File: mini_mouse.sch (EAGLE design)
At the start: 32 parts, among them IC1 PIC18F4550_TQFP, IC3 LP2950CDT-5.0, IC4 L293D

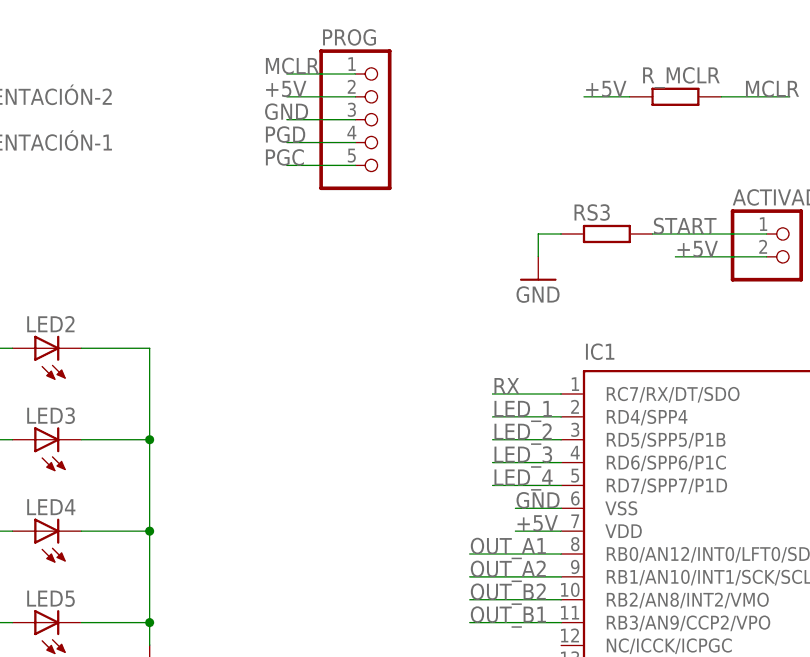
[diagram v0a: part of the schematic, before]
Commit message: Leds re-acomodados
Se  acomodaron los LEDS del lado derecho de la placa.
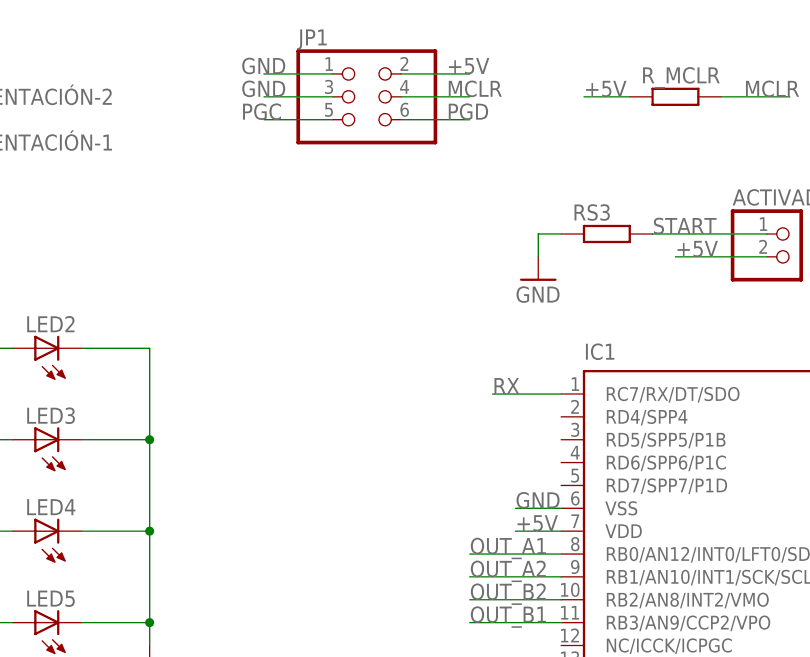
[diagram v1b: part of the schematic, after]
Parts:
- removed PROG: (no value), pinhead:PINHD-1X5
- added JP1: (no value), pinhead:PINHD-2X3
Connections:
- net +5V: now also JP1.2; no longer PROG.2
- net GND: now also JP1.1, JP1.3; no longer PROG.3
- net LED_1: no longer IC1.RD4/SPP4
- net LED_2: no longer IC1.RD5/SPP5/P1B
- net LED_3: no longer IC1.RD6/SPP6/P1C
- net LED_4: no longer IC1.RD7/SPP7/P1D
- net MCLR: now also JP1.4; no longer PROG.1
- net PGC: now also JP1.5; no longer PROG.5
- net PGD: now also JP1.6; no longer PROG.4
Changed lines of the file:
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@@
 <part name="C2" library="rcl" library_urn="urn:adsk.eagle:library:334" deviceset="C-EU" device="C0603" package3d_urn="urn:adsk.eagle:package:23616/2"/>
 <part name="R_MCLR" library="rcl" library_urn="urn:adsk.eagle:library:334" deviceset="R-EU_" device="R0603" package3d_urn="urn:adsk.eagle:package:23555/3"/>
-<part name="PROG" library="pinhead" library_urn="urn:adsk.eagle:library:325" deviceset="PINHD-1X5" device="" package3d_urn="urn:adsk.eagle:package:22469/2"/>
 <part name="GND1" library="supply1" library_urn="urn:adsk.eagle:library:371" deviceset="GND" device=""/>
 <part name="GND2" library="supply1" library_urn="urn:adsk.eagle:library:371" deviceset="GND" device=""/>
@@
 <part name="C4" library="rcl" library_urn="urn:adsk.eagle:library:334" deviceset="CPOL-EU" device="E5-6" package3d_urn="urn:adsk.eagle:package:23368/1"/>
 <part name="COMUNICACION" library="pinhead" library_urn="urn:adsk.eagle:library:325" deviceset="PINHD-2X2" device="" package3d_urn="urn:adsk.eagle:package:22455/2"/>
+<part name="JP1" library="pinhead" library_urn="urn:adsk.eagle:library:325" deviceset="PINHD-2X3" device="" package3d_urn="urn:adsk.eagle:package:22462/2"/>
 </parts>
 <sheets>
@@
 <attribute name="VALUE" x="107.95" y="156.718" size="1.778" layer="96"/>
 </instance>
-<instance part="PROG" gate="A" x="78.74" y="157.48">
-<attribute name="NAME" x="72.39" y="165.735" size="1.778" layer="95"/>
-<attribute name="VALUE" x="72.39" y="147.32" size="1.778" layer="96"/>
-</instance>
 <instance part="GND1" gate="1" x="12.7" y="149.86">
 <attribute name="VALUE" x="10.16" y="147.32" size="1.778" layer="96"/>
@@
 <attribute name="NAME" x="227.33" y="160.655" size="1.778" layer="95"/>
 <attribute name="VALUE" x="227.33" y="149.86" size="1.778" layer="96"/>
+</instance>
+<instance part="JP1" gate="A" x="76.2" y="160.02">
+<attribute name="NAME" x="69.85" y="165.735" size="1.778" layer="95"/>
+<attribute name="VALUE" x="69.85" y="152.4" size="1.778" layer="96"/>
 </instance>
 </instances>
@@
 <net name="MCLR" class="0">
 <segment>
-<pinref part="PROG" gate="A" pin="1"/>
-<wire x1="76.2" y1="162.56" x2="68.58" y2="162.56" width="0.1524" layer="91"/>
-<label x="66.04" y="162.56" size="1.778" layer="95"/>
-</segment>
-<segment>
 <pinref part="IC1" gate="G$1" pin="!MCLR!/VPP/RE3"/>
 <wire x1="99.06" y1="83.82" x2="91.44" y2="83.82" width="0.1524" layer="91"/>
@@
 <label x="119.38" y="160.02" size="1.778" layer="95"/>
 </segment>
+<segment>
+<pinref part="JP1" gate="A" pin="4"/>
+<wire x1="81.28" y1="160.02" x2="88.9" y2="160.02" width="0.1524" layer="91"/>
+<label x="86.36" y="160.02" size="1.778" layer="95"/>
+</segment>
 </net>
 <net name="+5V" class="0">
-<segment>
-<pinref part="PROG" gate="A" pin="2"/>
-<wire x1="76.2" y1="160.02" x2="68.58" y2="160.02" width="0.1524" layer="91"/>
-<label x="66.04" y="160.02" size="1.778" layer="95"/>
-</segment>
 <segment>
 <pinref part="IC1" gate="G$1" pin="VDD"/>
@@
 <label x="220.98" y="157.48" size="1.778" layer="95"/>
 </segment>
+<segment>
+<pinref part="JP1" gate="A" pin="2"/>
+<wire x1="81.28" y1="162.56" x2="88.9" y2="162.56" width="0.1524" layer="91"/>
+<label x="86.36" y="162.56" size="1.778" layer="95"/>
+</segment>
 </net>
 <net name="PGD" class="0">
-<segment>
-<pinref part="PROG" gate="A" pin="4"/>
-<wire x1="76.2" y1="154.94" x2="68.58" y2="154.94" width="0.1524" layer="91"/>
-<label x="66.04" y="154.94" size="1.778" layer="95"/>
-</segment>
 <segment>
 <pinref part="IC1" gate="G$1" pin="RB7/BKI3/PGD"/>
@@
 <label x="91.44" y="86.36" size="1.778" layer="95"/>
 </segment>
+<segment>
+<pinref part="JP1" gate="A" pin="6"/>
+<wire x1="81.28" y1="157.48" x2="88.9" y2="157.48" width="0.1524" layer="91"/>
+<label x="86.36" y="157.48" size="1.778" layer="95"/>
+</segment>
 </net>
 <net name="PGC" class="0">
-<segment>
-<pinref part="PROG" gate="A" pin="5"/>
-<wire x1="76.2" y1="152.4" x2="68.58" y2="152.4" width="0.1524" layer="91"/>
-<label x="66.04" y="152.4" size="1.778" layer="95"/>
-</segment>
 <segment>
 <pinref part="IC1" gate="G$1" pin="RB6/KBI2/PGC"/>
 <wire x1="99.06" y1="88.9" x2="91.44" y2="88.9" width="0.1524" layer="91"/>
 <label x="91.44" y="88.9" size="1.778" layer="95"/>
+</segment>
+<segment>
+<pinref part="JP1" gate="A" pin="5"/>
+<wire x1="73.66" y1="157.48" x2="66.04" y2="157.48" width="0.1524" layer="91"/>
+<label x="63.5" y="157.48" size="1.778" layer="95"/>
 </segment>
 </net>
@@
 <wire x1="152.4" y1="149.86" x2="152.4" y2="152.4" width="0.1524" layer="91"/>
 <junction x="152.4" y="152.4"/>
-</segment>
-<segment>
-<pinref part="PROG" gate="A" pin="3"/>
-<wire x1="76.2" y1="157.48" x2="68.58" y2="157.48" width="0.1524" layer="91"/>
-<label x="66.04" y="157.48" size="1.778" layer="95"/>
 </segment>
 <segment>
@@
 <label x="220.98" y="154.94" size="1.778" layer="95"/>
 </segment>
+<segment>
+<pinref part="JP1" gate="A" pin="1"/>
+<wire x1="73.66" y1="162.56" x2="66.04" y2="162.56" width="0.1524" layer="91"/>
+<label x="63.5" y="162.56" size="1.778" layer="95"/>
+</segment>
+<segment>
+<pinref part="JP1" gate="A" pin="3"/>
+<wire x1="73.66" y1="160.02" x2="66.04" y2="160.02" width="0.1524" layer="91"/>
+<label x="63.5" y="160.02" size="1.778" layer="95"/>
+</segment>
 </net>
 <net name="OSC2" class="0">
@@
 <net name="LED_1" class="0">
 <segment>
-<pinref part="IC1" gate="G$1" pin="RD4/SPP4"/>
-<wire x1="99.06" y1="124.46" x2="91.44" y2="124.46" width="0.1524" layer="91"/>
-<label x="91.44" y="124.46" size="1.778" layer="95"/>
-</segment>
-<segment>
 <pinref part="R_L1" gate="G$1" pin="1"/>
 <wire x1="22.86" y1="132.08" x2="17.78" y2="132.08" width="0.1524" layer="91"/>
@@
 <net name="LED_2" class="0">
 <segment>
-<pinref part="IC1" gate="G$1" pin="RD5/SPP5/P1B"/>
-<wire x1="99.06" y1="121.92" x2="91.44" y2="121.92" width="0.1524" layer="91"/>
-<label x="91.44" y="121.92" size="1.778" layer="95"/>
-</segment>
-<segment>
 <pinref part="R_L2" gate="G$1" pin="1"/>
 <wire x1="22.86" y1="121.92" x2="17.78" y2="121.92" width="0.1524" layer="91"/>
@@
 <net name="LED_3" class="0">
 <segment>
-<pinref part="IC1" gate="G$1" pin="RD6/SPP6/P1C"/>
-<wire x1="99.06" y1="119.38" x2="91.44" y2="119.38" width="0.1524" layer="91"/>
-<label x="91.44" y="119.38" size="1.778" layer="95"/>
-</segment>
-<segment>
 <pinref part="R_L3" gate="G$1" pin="1"/>
 <wire x1="22.86" y1="111.76" x2="17.78" y2="111.76" width="0.1524" layer="91"/>
@@
 <net name="LED_4" class="0">
 <segment>
-<pinref part="IC1" gate="G$1" pin="RD7/SPP7/P1D"/>
-<wire x1="99.06" y1="116.84" x2="91.44" y2="116.84" width="0.1524" layer="91"/>
-<label x="91.44" y="116.84" size="1.778" layer="95"/>
-</segment>
-<segment>
 <pinref part="R_L4" gate="G$1" pin="1"/>

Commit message: Actualización Board
Se actualizo la distribucion de componentes, se cambio el tamaño de los package de las resistencias y capacitores smd y se modifico la forma de la tarjeta.
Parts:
- removed ALIMENTACIÓN: (no value), con-wago-500:W237-102
- added JP3: (no value), pinhead:PINHD-1X2
- C1, C2: device rcl:C-EUC0603 -> rcl:R-EU_R0805
- RS1, RS2, RS3, R_L1, R_L2, R_L3, R_L4, R_MCLR: device rcl:R-EU_R0603 -> rcl:R-EU_R0805
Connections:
- net BAT: now also JP3.1; no longer ALIMENTACIÓN-2.KL
- net N$5: now also JP3.2; no longer ALIMENTACIÓN-1.KL
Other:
- moved on the sheet: C1, C2
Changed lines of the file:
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@@
 <part name="IC1" library="microchip" library_urn="urn:adsk.eagle:library:294" deviceset="PIC18F4*_TQFP" device="" package3d_urn="urn:adsk.eagle:package:20793/2" technology="550"/>
 <part name="Q1" library="crystal" library_urn="urn:adsk.eagle:library:204" deviceset="CRYSTAL" device="HC49U-V" package3d_urn="urn:adsk.eagle:package:12075/1"/>
-<part name="C1" library="rcl" library_urn="urn:adsk.eagle:library:334" deviceset="C-EU" device="C0603" package3d_urn="urn:adsk.eagle:package:23616/2"/>
-<part name="C2" library="rcl" library_urn="urn:adsk.eagle:library:334" deviceset="C-EU" device="C0603" package3d_urn="urn:adsk.eagle:package:23616/2"/>
-<part name="R_MCLR" library="rcl" library_urn="urn:adsk.eagle:library:334" deviceset="R-EU_" device="R0603" package3d_urn="urn:adsk.eagle:package:23555/3"/>
+<part name="C1" library="rcl" library_urn="urn:adsk.eagle:library:334" deviceset="R-EU_" device="R0805" package3d_urn="urn:adsk.eagle:package:23553/2"/>
+<part name="C2" library="rcl" library_urn="urn:adsk.eagle:library:334" deviceset="R-EU_" device="R0805" package3d_urn="urn:adsk.eagle:package:23553/2"/>
+<part name="R_MCLR" library="rcl" library_urn="urn:adsk.eagle:library:334" deviceset="R-EU_" device="R0805" package3d_urn="urn:adsk.eagle:package:23553/2"/>
 <part name="GND1" library="supply1" library_urn="urn:adsk.eagle:library:371" deviceset="GND" device=""/>
 <part name="GND2" library="supply1" library_urn="urn:adsk.eagle:library:371" deviceset="GND" device=""/>
-<part name="R_L1" library="rcl" library_urn="urn:adsk.eagle:library:334" deviceset="R-EU_" device="R0603" package3d_urn="urn:adsk.eagle:package:23555/3"/>
-<part name="R_L2" library="rcl" library_urn="urn:adsk.eagle:library:334" deviceset="R-EU_" device="R0603" package3d_urn="urn:adsk.eagle:package:23555/3"/>
-<part name="R_L3" library="rcl" library_urn="urn:adsk.eagle:library:334" deviceset="R-EU_" device="R0603" package3d_urn="urn:adsk.eagle:package:23555/3"/>
-<part name="R_L4" library="rcl" library_urn="urn:adsk.eagle:library:334" deviceset="R-EU_" device="R0603" package3d_urn="urn:adsk.eagle:package:23555/3"/>
+<part name="R_L1" library="rcl" library_urn="urn:adsk.eagle:library:334" deviceset="R-EU_" device="R0805" package3d_urn="urn:adsk.eagle:package:23553/2"/>
+<part name="R_L2" library="rcl" library_urn="urn:adsk.eagle:library:334" deviceset="R-EU_" device="R0805" package3d_urn="urn:adsk.eagle:package:23553/2"/>
+<part name="R_L3" library="rcl" library_urn="urn:adsk.eagle:library:334" deviceset="R-EU_" device="R0805" package3d_urn="urn:adsk.eagle:package:23553/2"/>
+<part name="R_L4" library="rcl" library_urn="urn:adsk.eagle:library:334" deviceset="R-EU_" device="R0805" package3d_urn="urn:adsk.eagle:package:23553/2"/>
 <part name="GND3" library="supply1" library_urn="urn:adsk.eagle:library:371" deviceset="GND" device=""/>
 <part name="LED2" library="led" library_urn="urn:adsk.eagle:library:259" deviceset="LED" device="3MM" package3d_urn="urn:adsk.eagle:package:15797/1"/>
@@
 <part name="LED4" library="led" library_urn="urn:adsk.eagle:library:259" deviceset="LED" device="3MM" package3d_urn="urn:adsk.eagle:package:15797/1"/>
 <part name="LED5" library="led" library_urn="urn:adsk.eagle:library:259" deviceset="LED" device="3MM" package3d_urn="urn:adsk.eagle:package:15797/1"/>
-<part name="ALIMENTACIÓN" library="con-wago-500" library_urn="urn:adsk.eagle:library:195" deviceset="W237-102" device="" package3d_urn="urn:adsk.eagle:package:10688/1"/>
 <part name="ENCODER_1" library="pinhead" library_urn="urn:adsk.eagle:library:325" deviceset="PINHD-1X6" device="" package3d_urn="urn:adsk.eagle:package:22472/2"/>
 <part name="ENCODER_2" library="pinhead" library_urn="urn:adsk.eagle:library:325" deviceset="PINHD-1X6" device="" package3d_urn="urn:adsk.eagle:package:22472/2"/>
 <part name="OPCIONES" library="switch-dil" library_urn="urn:adsk.eagle:library:375" deviceset="DIP02YL" device="" package3d_urn="urn:adsk.eagle:package:27254/2"/>
-<part name="RS1" library="rcl" library_urn="urn:adsk.eagle:library:334" deviceset="R-EU_" device="R0603" package3d_urn="urn:adsk.eagle:package:23555/3"/>
-<part name="RS2" library="rcl" library_urn="urn:adsk.eagle:library:334" deviceset="R-EU_" device="R0603" package3d_urn="urn:adsk.eagle:package:23555/3"/>
+<part name="RS1" library="rcl" library_urn="urn:adsk.eagle:library:334" deviceset="R-EU_" device="R0805" package3d_urn="urn:adsk.eagle:package:23553/2"/>
+<part name="RS2" library="rcl" library_urn="urn:adsk.eagle:library:334" deviceset="R-EU_" device="R0805" package3d_urn="urn:adsk.eagle:package:23553/2"/>
 <part name="GND4" library="supply1" library_urn="urn:adsk.eagle:library:371" deviceset="GND" device=""/>
 <part name="P+2" library="supply1" library_urn="urn:adsk.eagle:library:371" deviceset="+5V" device=""/>
@@
 <part name="JP2" library="pinhead" library_urn="urn:adsk.eagle:library:325" deviceset="PINHD-1X2" device="" package3d_urn="urn:adsk.eagle:package:22435/2"/>
 <part name="ACTIVADOR" library="pinhead" library_urn="urn:adsk.eagle:library:325" deviceset="PINHD-1X2" device="" package3d_urn="urn:adsk.eagle:package:22435/2"/>
-<part name="RS3" library="rcl" library_urn="urn:adsk.eagle:library:334" deviceset="R-EU_" device="R0603" package3d_urn="urn:adsk.eagle:package:23555/3"/>
+<part name="RS3" library="rcl" library_urn="urn:adsk.eagle:library:334" deviceset="R-EU_" device="R0805" package3d_urn="urn:adsk.eagle:package:23553/2"/>
 <part name="GND6" library="supply1" library_urn="urn:adsk.eagle:library:371" deviceset="GND" device=""/>
 <part name="IC4" library="st-microelectronics" library_urn="urn:adsk.eagle:library:368" deviceset="L293D" device="" package3d_urn="urn:adsk.eagle:package:26820/1"/>
@@
 <part name="COMUNICACION" library="pinhead" library_urn="urn:adsk.eagle:library:325" deviceset="PINHD-2X2" device="" package3d_urn="urn:adsk.eagle:package:22455/2"/>
 <part name="JP1" library="pinhead" library_urn="urn:adsk.eagle:library:325" deviceset="PINHD-2X3" device="" package3d_urn="urn:adsk.eagle:package:22462/2"/>
+<part name="JP3" library="pinhead" library_urn="urn:adsk.eagle:library:325" deviceset="PINHD-1X2" device="" package3d_urn="urn:adsk.eagle:package:22435/2"/>
 </parts>
 <sheets>
@@
 <attribute name="VALUE" x="45.212" y="107.315" size="1.778" layer="96" rot="R180"/>
 </instance>
-<instance part="ALIMENTACIÓN" gate="-1" x="30.48" y="154.94" rot="R180">
-<attribute name="NAME" x="30.48" y="154.051" size="1.778" layer="95"/>
-</instance>
-<instance part="ALIMENTACIÓN" gate="-2" x="30.48" y="160.02" rot="R180">
-<attribute name="VALUE" x="33.02" y="163.703" size="1.778" layer="96" rot="R180"/>
-<attribute name="NAME" x="30.48" y="159.131" size="1.778" layer="95"/>
-</instance>
 <instance part="ENCODER_1" gate="A" x="43.18" y="68.58">
 <attribute name="NAME" x="36.83" y="79.375" size="1.778" layer="95"/>
@@
 <attribute name="NAME" x="69.85" y="165.735" size="1.778" layer="95"/>
 <attribute name="VALUE" x="69.85" y="152.4" size="1.778" layer="96"/>
+</instance>
+<instance part="JP3" gate="G$1" x="38.1" y="157.48">
+<attribute name="NAME" x="31.75" y="163.195" size="1.778" layer="95"/>
+<attribute name="VALUE" x="31.75" y="152.4" size="1.778" layer="96"/>
 </instance>
 </instances>
@@
 <segment>
 <pinref part="C1" gate="G$1" pin="2"/>
-<wire x1="144.78" y1="154.94" x2="144.78" y2="152.4" width="0.1524" layer="91"/>
+<wire x1="149.86" y1="160.02" x2="144.78" y2="152.4" width="0.1524" layer="91"/>
 <wire x1="144.78" y1="152.4" x2="152.4" y2="152.4" width="0.1524" layer="91"/>
 <pinref part="C2" gate="G$1" pin="2"/>
 <wire x1="152.4" y1="152.4" x2="160.02" y2="152.4" width="0.1524" layer="91"/>
-<wire x1="160.02" y1="152.4" x2="160.02" y2="154.94" width="0.1524" layer="91"/>
+<wire x1="160.02" y1="152.4" x2="165.1" y2="160.02" width="0.1524" layer="91"/>
 <pinref part="GND2" gate="1" pin="GND"/>
 <wire x1="152.4" y1="149.86" x2="152.4" y2="152.4" width="0.1524" layer="91"/>
@@
 <wire x1="154.94" y1="165.1" x2="160.02" y2="165.1" width="0.1524" layer="91"/>
 <pinref part="C2" gate="G$1" pin="1"/>
-<wire x1="160.02" y1="165.1" x2="160.02" y2="162.56" width="0.1524" layer="91"/>
+<wire x1="160.02" y1="165.1" x2="154.94" y2="160.02" width="0.1524" layer="91"/>
 <label x="160.02" y="165.1" size="1.778" layer="95"/>
 </segment>
@@
 <segment>
 <pinref part="C1" gate="G$1" pin="1"/>
-<wire x1="144.78" y1="162.56" x2="144.78" y2="165.1" width="0.1524" layer="91"/>
+<wire x1="139.7" y1="160.02" x2="144.78" y2="165.1" width="0.1524" layer="91"/>
 <pinref part="Q1" gate="G$1" pin="1"/>
 <wire x1="144.78" y1="165.1" x2="149.86" y2="165.1" width="0.1524" layer="91"/>
@@
 <segment>
 <label x="15.24" y="160.02" size="1.778" layer="95"/>
-<pinref part="ALIMENTACIÓN" gate="-2" pin="KL"/>
-<wire x1="12.7" y1="160.02" x2="25.4" y2="160.02" width="0.1524" layer="91"/>
+<wire x1="12.7" y1="160.02" x2="35.56" y2="160.02" width="0.1524" layer="91"/>
+<pinref part="JP3" gate="G$1" pin="1"/>
 </segment>
 <segment>
@@
 <segment>
 <pinref part="JP2" gate="G$1" pin="1"/>
-<pinref part="ALIMENTACIÓN" gate="-1" pin="KL"/>
-<wire x1="25.4" y1="154.94" x2="25.4" y2="147.32" width="0.1524" layer="91"/>
+<wire x1="25.4" y1="157.48" x2="25.4" y2="147.32" width="0.1524" layer="91"/>
 <wire x1="25.4" y1="147.32" x2="27.94" y2="147.32" width="0.1524" layer="91"/>
-</segment>
-</net>
+<pinref part="JP3" gate="G$1" pin="2"/>
+<wire x1="35.56" y1="157.48" x2="25.4" y2="157.48" width="0.1524" layer="91"/>
+</segment>
+</net>

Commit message: Final Designe
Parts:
- C3, C4: device rcl:CPOL-EUE5-6 -> rcl:CPOL-EUE2-4
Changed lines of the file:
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@@
 <part name="GND7" library="supply1" library_urn="urn:adsk.eagle:library:371" deviceset="GND" device=""/>
 <part name="GND8" library="supply1" library_urn="urn:adsk.eagle:library:371" deviceset="GND" device=""/>
-<part name="C3" library="rcl" library_urn="urn:adsk.eagle:library:334" deviceset="CPOL-EU" device="E5-6" package3d_urn="urn:adsk.eagle:package:23368/1"/>
-<part name="C4" library="rcl" library_urn="urn:adsk.eagle:library:334" deviceset="CPOL-EU" device="E5-6" package3d_urn="urn:adsk.eagle:package:23368/1"/>
+<part name="C3" library="rcl" library_urn="urn:adsk.eagle:library:334" deviceset="CPOL-EU" device="E2-4" package3d_urn="urn:adsk.eagle:package:23347/1"/>
+<part name="C4" library="rcl" library_urn="urn:adsk.eagle:library:334" deviceset="CPOL-EU" device="E2-4" package3d_urn="urn:adsk.eagle:package:23347/1"/>
 <part name="COMUNICACION" library="pinhead" library_urn="urn:adsk.eagle:library:325" deviceset="PINHD-2X2" device="" package3d_urn="urn:adsk.eagle:package:22455/2"/>
 <part name="JP1" library="pinhead" library_urn="urn:adsk.eagle:library:325" deviceset="PINHD-2X3" device="" package3d_urn="urn:adsk.eagle:package:22462/2"/>
